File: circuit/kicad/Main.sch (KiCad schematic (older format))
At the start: 104 parts, among them J1 SH3, J10 PA3, J11 SH4, J2 SH3, J3 FFC6, J4 SH6, J5 FTSH2x5, J6 FFC4, J7 SH4, J8 FFC12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

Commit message: フットプリントの問題は解消
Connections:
- wire segments 428 -> 432
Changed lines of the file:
@@
-	1    0    0    -1
-$EndComp
-$Comp
-L power:+3.3V #PWR063
-U 1 1 62009803
-P 8950 7050
-AR Path="/62009803" Ref="#PWR063"  Part="1"
-AR Path="/624FCD7A/62009803" Ref="#PWR?"  Part="1"
-AR Path="/61F602DC/62009803" Ref="#PWR?"  Part="1"
-AR Path="/61F60664/62009803" Ref="#PWR?"  Part="1"
-F 0 "#PWR063" H 8950 6900 50  0001 C CNN
-F 1 "+3.3V" H 8965 7223 50  0000 C CNN
-F 2 "" H 8950 7050 50  0001 C CNN
-F 3 "" H 8950 7050 50  0001 C CNN
-	1    8950 7050
-	1    0    0    -1
-$EndComp
-$Comp
-L power:GND #PWR066
-U 1 1 6200980A
-P 8950 7950
-AR Path="/6200980A" Ref="#PWR066"  Part="1"
-AR Path="/624FCD7A/6200980A" Ref="#PWR?"  Part="1"
-AR Path="/61F602DC/6200980A" Ref="#PWR?"  Part="1"
-AR Path="/61F60664/6200980A" Ref="#PWR?"  Part="1"
-F 0 "#PWR066" H 8950 7700 50  0001 C CNN
-F 1 "GND" H 8955 7777 50  0000 C CNN
-F 2 "" H 8950 7950 50  0001 C CNN
-F 3 "" H 8950 7950 50  0001 C CNN
-	1    8950 7950
 	1    0    0    -1
 $EndComp
@@
 Text Notes 6850 6750 0    50   ~ 0
 240mA\n
-Text Notes 9450 7450 0    200  ~ 0
+Text Notes 9750 7450 0    200  ~ 0
 Buzzer
 Text Notes 4000 7100 2    200  ~ 0
@@
 	4250 7200 4250 7300
 Wire Wire Line
-	8950 7750 8950 7950
-Wire Wire Line
 	6250 8350 4800 8350
 Wire Wire Line
@@
 	7750 10350 7650 10350
 Wire Wire Line
-	8950 7050 8950 7250
+	9500 7700 9500 7900
 Wire Wire Line
 	6150 9450 6250 9450
@@
 Text Notes 850  1500 0    500  ~ 0
 Main
+Wire Wire Line
+	9500 7050 9500 7250
+$Comp
+L power:+3.3V #PWR063
+U 1 1 62009803
+P 9500 7700
+AR Path="/62009803" Ref="#PWR063"  Part="1"
+AR Path="/624FCD7A/62009803" Ref="#PWR?"  Part="1"
+AR Path="/61F602DC/62009803" Ref="#PWR?"  Part="1"
+AR Path="/61F60664/62009803" Ref="#PWR?"  Part="1"
+F 0 "#PWR063" H 9500 7550 50  0001 C CNN
+F 1 "+3.3V" H 9515 7873 50  0000 C CNN
+F 2 "" H 9500 7700 50  0001 C CNN
+F 3 "" H 9500 7700 50  0001 C CNN
+	1    9500 7700
+	1    0    0    -1
+$EndComp
+$Comp
+L power:GND #PWR066
+U 1 1 6200980A
+P 9500 7250
+AR Path="/6200980A" Ref="#PWR066"  Part="1"
+AR Path="/624FCD7A/6200980A" Ref="#PWR?"  Part="1"
+AR Path="/61F602DC/6200980A" Ref="#PWR?"  Part="1"
+AR Path="/61F60664/6200980A" Ref="#PWR?"  Part="1"
+F 0 "#PWR066" H 9500 7000 50  0001 C CNN
+F 1 "GND" H 9505 7077 50  0000 C CNN
+F 2 "" H 9500 7250 50  0001 C CNN
+F 3 "" H 9500 7250 50  0001 C CNN
+	1    9500 7250
+	1    0    0    -1
+$EndComp
+Wire Wire Line
+	9500 7900 8950 7900
+Wire Wire Line
+	8950 7900 8950 7750
+Wire Wire Line
+	9500 7050 8950 7050
+Wire Wire Line
+	8950 7050 8950 7250
 Wire Bus Line
 	19750 5950 19750 8850

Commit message: タイヤをギアと一体化させた
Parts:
- SW1: symbol SKRPABE010:Switch -> Main-rescue:Switch-SKRPABE010
- U1: symbol OSC:ASTMLPA-16MHz-LJ-E-T -> Main-rescue:ASTMLPA-16MHz-LJ-E-T-OSC
- U2: symbol MCU_ST_STM32F4:STM32F405RGTx -> Main-rescue:STM32F405RGTx-MCU_ST_STM32F4
- U3: symbol ICM-20648:ICM-20648 -> Main-rescue:ICM-20648-ICM-20648
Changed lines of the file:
@@
 ICM_SCLK
 $Comp
-L ICM-20648:ICM-20648 U3
+L Main-rescue:ICM-20648-ICM-20648 U3
 U 1 1 620093A0
 P 17800 12000
@@
 USART
 $Comp
-L OSC:ASTMLPA-16MHz-LJ-E-T U1
+L Main-rescue:ASTMLPA-16MHz-LJ-E-T-OSC U1
 U 1 1 62009950
 P 4250 7600
@@
 	8200 7850 7650 7850
 $Comp
-L MCU_ST_STM32F4:STM32F405RGTx U2
+L Main-rescue:STM32F405RGTx-MCU_ST_STM32F4 U2
 U 1 1 62009A8F
 P 6950 8750
@@
 	5200 6900 5800 6900
 $Comp
-L SKRPABE010:Switch SW?
+L Main-rescue:Switch-SKRPABE010 SW?
 U 1 1 62009AD1
 P 5200 7200

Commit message: hoge
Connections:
- net DRV1_EN: now also J6.2 (Pin_2), U2.58 (PB6); no longer J6.1 (Pin_1), U2.54 (PD2)
- net DRV1_PN: now also J6.1 (Pin_1), U2.54 (PD2); no longer J6.2 (Pin_2), U2.58 (PB6)
- net DRV2_EN: now also J6.3 (Pin_3), U2.59 (PB7); no longer J6.4 (Pin_4), U2.2 (PC13)
- net DRV2_PN: now also J6.4 (Pin_4), U2.2 (PC13); no longer J6.3 (Pin_3), U2.59 (PB7)
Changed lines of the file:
@@
 	1    0    0    -1
 $EndComp
-Text Label 9000 12100 0    50   ~ 0
-DRV1_EN
-Text Label 9000 12200 0    50   ~ 0
-DRV1_PN
-Text Label 9000 12400 0    50   ~ 0
-DRV2_EN
-Text Label 9000 12300 0    50   ~ 0
-DRV2_PN
 Text Label 9000 13400 0    50   ~ 0
 Rotary1
@@
 	8800 9550 8900 9650
 Text Label 8800 9450 2    50   ~ 0
-DRV1_PN
+DRV1_EN
 Text Label 8800 9550 2    50   ~ 0
-DRV2_PN
+DRV2_EN
 Wire Wire Line
 	7650 9550 8800 9550
@@
 	7650 9350 7750 9350
 Text Label 5300 8650 0    50   ~ 0
-DRV1_EN
+DRV1_PN
 Wire Wire Line
 	5300 8650 6250 8650
@@
 	4700 11000 8300 11000
 Text Label 5300 10150 0    50   ~ 0
-DRV2_EN
+DRV2_PN
 Wire Wire Line
 	5300 8450 6250 8450
@@
 Wire Bus Line
 	8900 11200 8900 13600
+Text Label 9000 12100 0    50   ~ 0
+DRV1_PN
+Text Label 9000 12200 0    50   ~ 0
+DRV1_EN
+Text Label 9000 12300 0    50   ~ 0
+DRV2_EN
+Text Label 9000 12400 0    50   ~ 0
+DRV2_PN
 $EndSCHEMATC

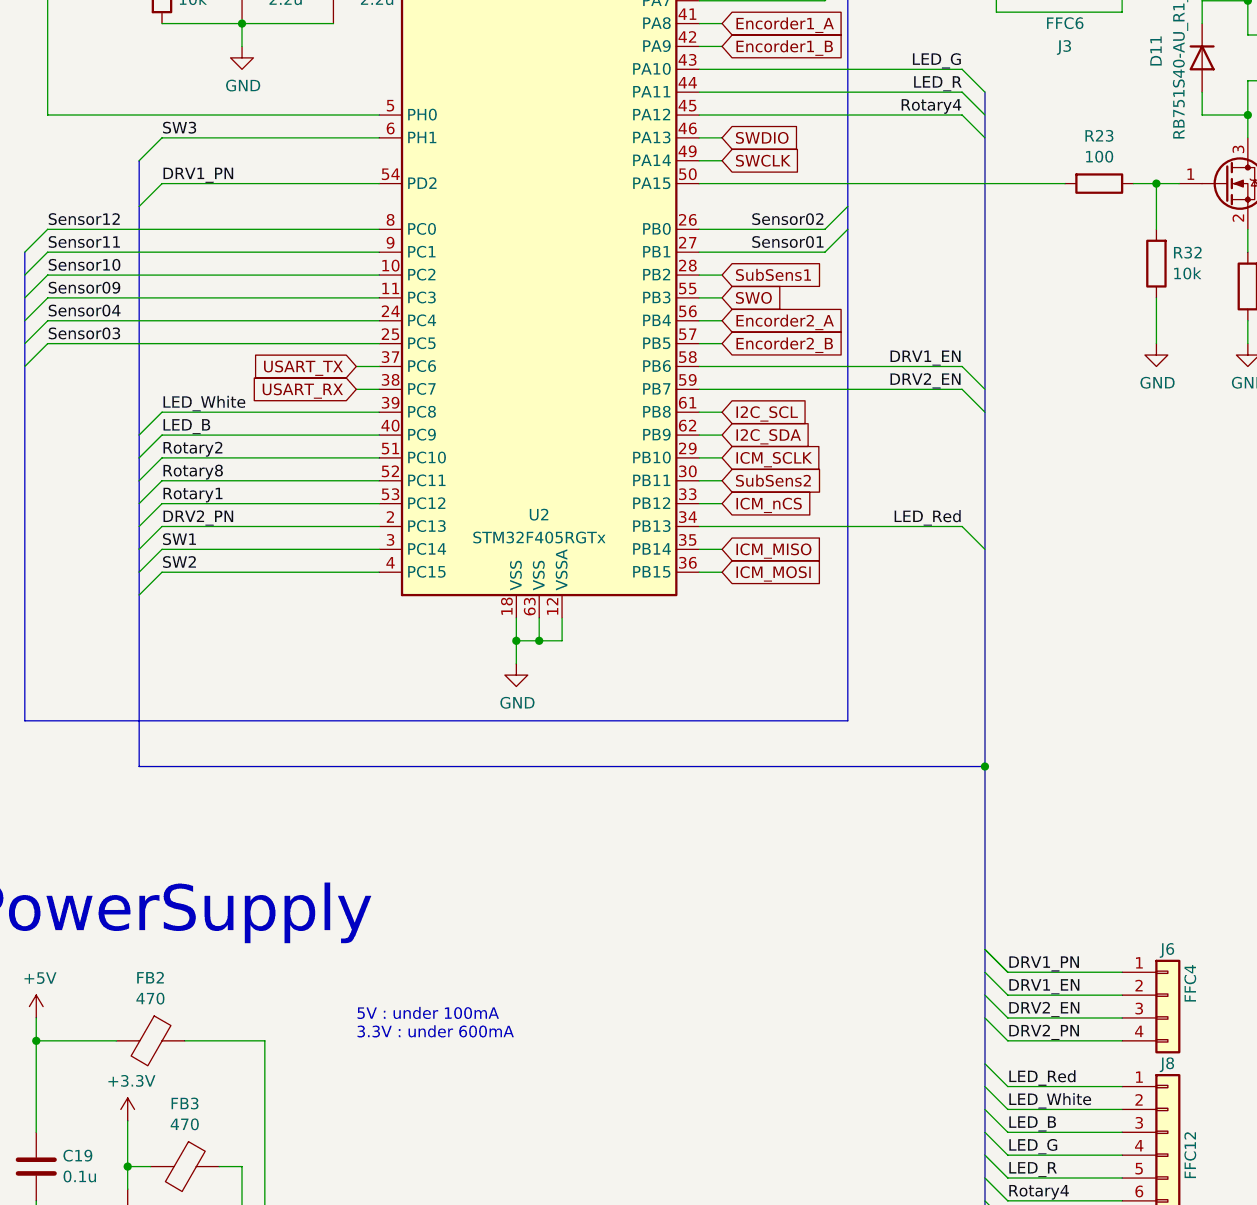
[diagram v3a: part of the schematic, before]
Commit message: P 制御するプログラムを実装（まだ実機で実験してないけど...
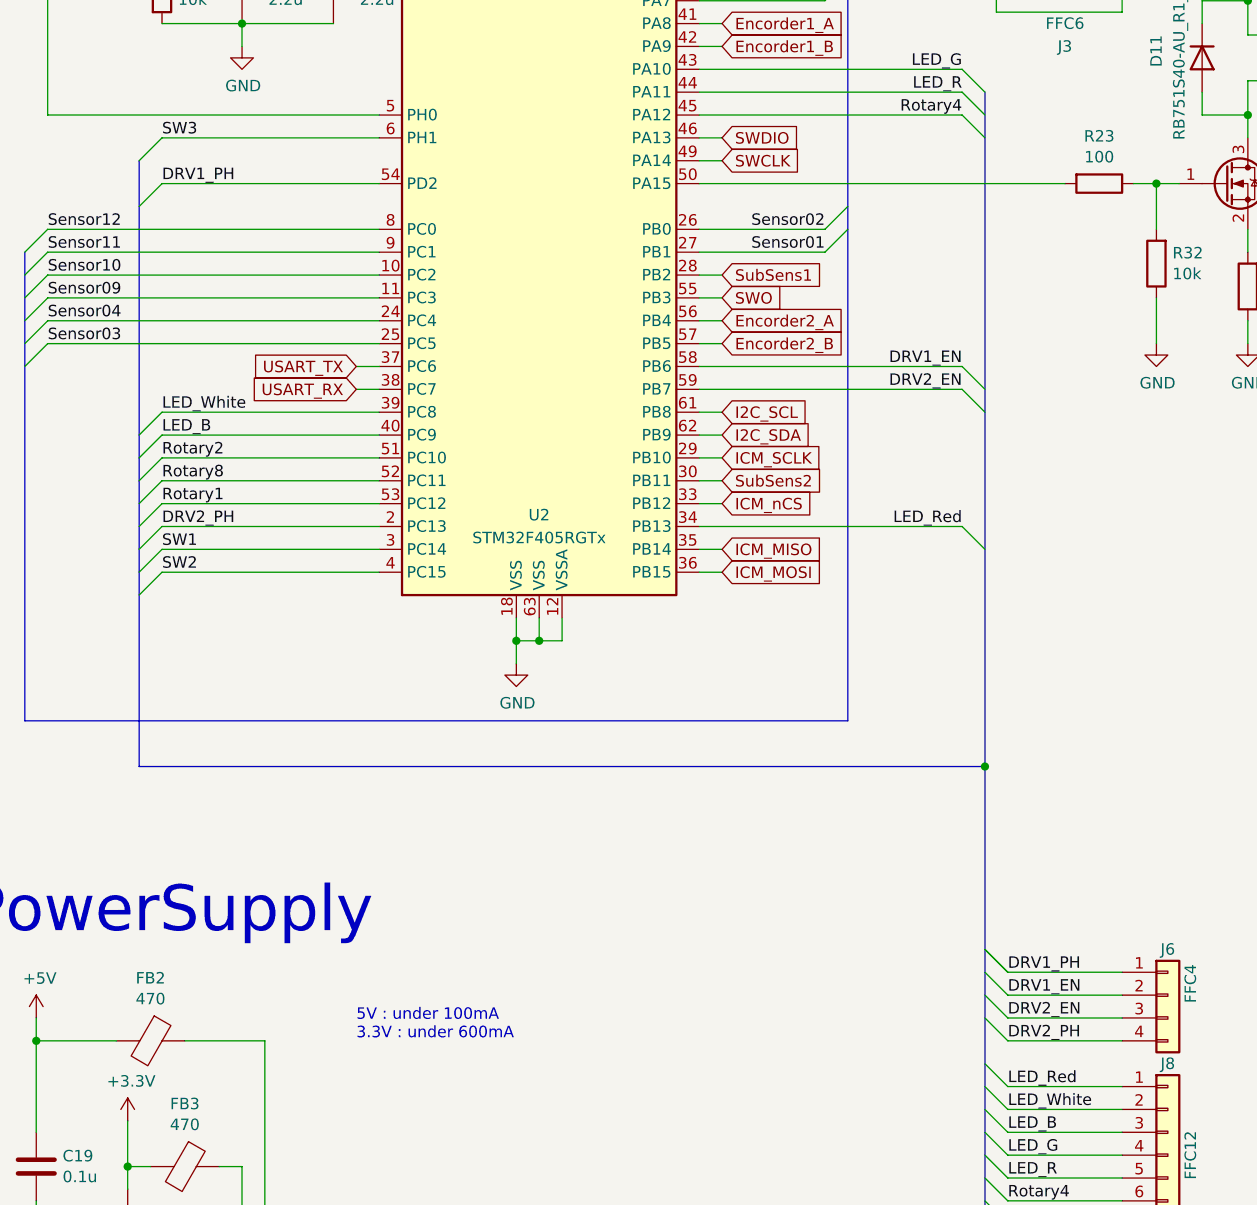
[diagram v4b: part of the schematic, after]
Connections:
- net DRV1_PN renamed DRV1_PH
- net DRV2_PN renamed DRV2_PH
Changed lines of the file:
@@
 	7650 9350 7750 9350
 Text Label 5300 8650 0    50   ~ 0
-DRV1_PN
+DRV1_PH
 Wire Wire Line
 	5300 8650 6250 8650
@@
 	4700 11000 8300 11000
 Text Label 5300 10150 0    50   ~ 0
-DRV2_PN
+DRV2_PH
 Wire Wire Line
 	5300 8450 6250 8450
@@
 Wire Wire Line
 	8950 7050 8950 7250
-Wire Bus Line
-	19750 5950 19750 8850
-Wire Bus Line
-	17750 5950 17750 8850
-Wire Bus Line
-	15750 5950 15750 8850
-Wire Bus Line
-	19750 2750 19750 5750
-Wire Bus Line
-	17750 2750 17750 5750
-Wire Bus Line
-	15750 2750 15750 5750
-Wire Bus Line
-	8300 5850 19650 5850
-Wire Bus Line
-	8300 5850 8300 11000
-Wire Bus Line
-	8900 8250 8900 11200
-Wire Bus Line
-	4700 8950 4700 11000
-Wire Bus Line
-	5200 8550 5200 11200
-Wire Bus Line
-	8900 11200 8900 13600
 Text Label 9000 12100 0    50   ~ 0
-DRV1_PN
+DRV1_PH
 Text Label 9000 12200 0    50   ~ 0
 DRV1_EN
@@
 DRV2_EN
 Text Label 9000 12400 0    50   ~ 0
-DRV2_PN
+DRV2_PH
+Wire Bus Line
+	19750 5950 19750 8850
+Wire Bus Line
+	17750 5950 17750 8850
+Wire Bus Line
+	15750 5950 15750 8850
+Wire Bus Line
+	19750 2750 19750 5750
+Wire Bus Line
+	17750 2750 17750 5750
+Wire Bus Line
+	15750 2750 15750 5750
+Wire Bus Line
+	8300 5850 19650 5850
+Wire Bus Line
+	8300 5850 8300 11000
+Wire Bus Line
+	8900 8250 8900 11200
+Wire Bus Line
+	4700 8950 4700 11000
+Wire Bus Line
+	5200 8550 5200 11200
+Wire Bus Line
+	8900 11200 8900 13600
 $EndSCHEMATC
